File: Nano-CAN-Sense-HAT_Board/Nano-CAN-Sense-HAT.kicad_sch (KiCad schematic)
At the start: 42 parts, among them J1 Analog, J2 Digital, J3 Conn_02x04_Counter_Clockwise, J4 Conn_02x04_Counter_Clockwise, J5 Conn_01x05, J6 Conn_01x03, SW1 SW_Push, SW2 SW_Push, U1 LMC6484, U2 MCP2518FD-xQBB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

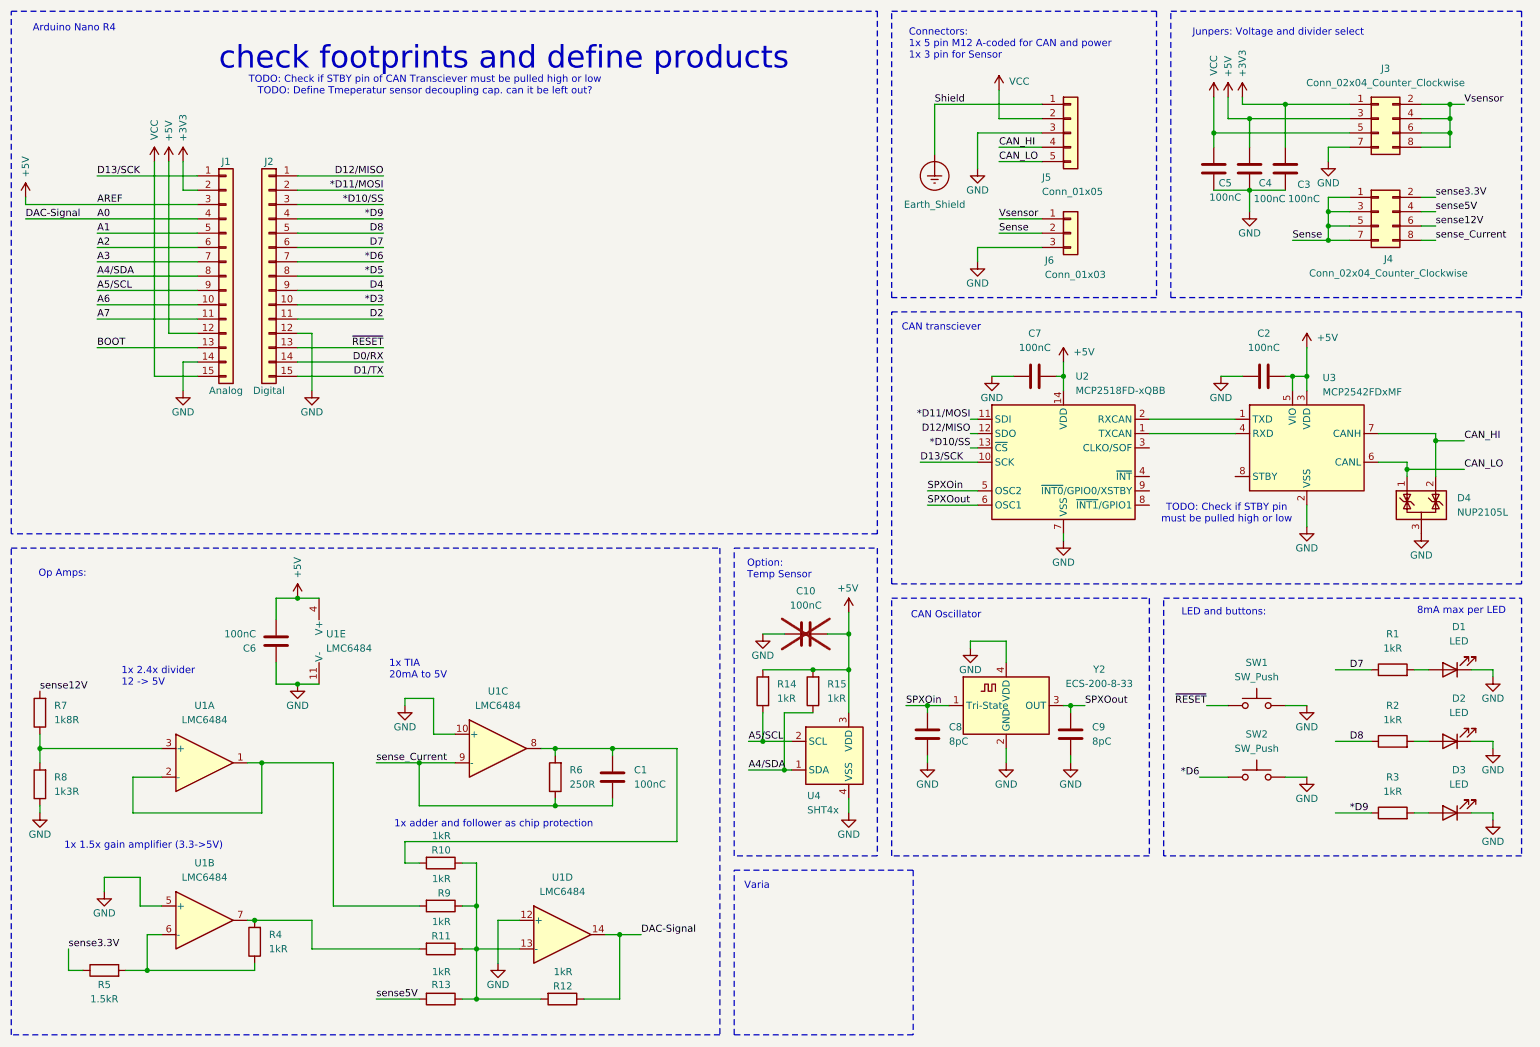
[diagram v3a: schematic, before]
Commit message: Added BOM, defined footprints
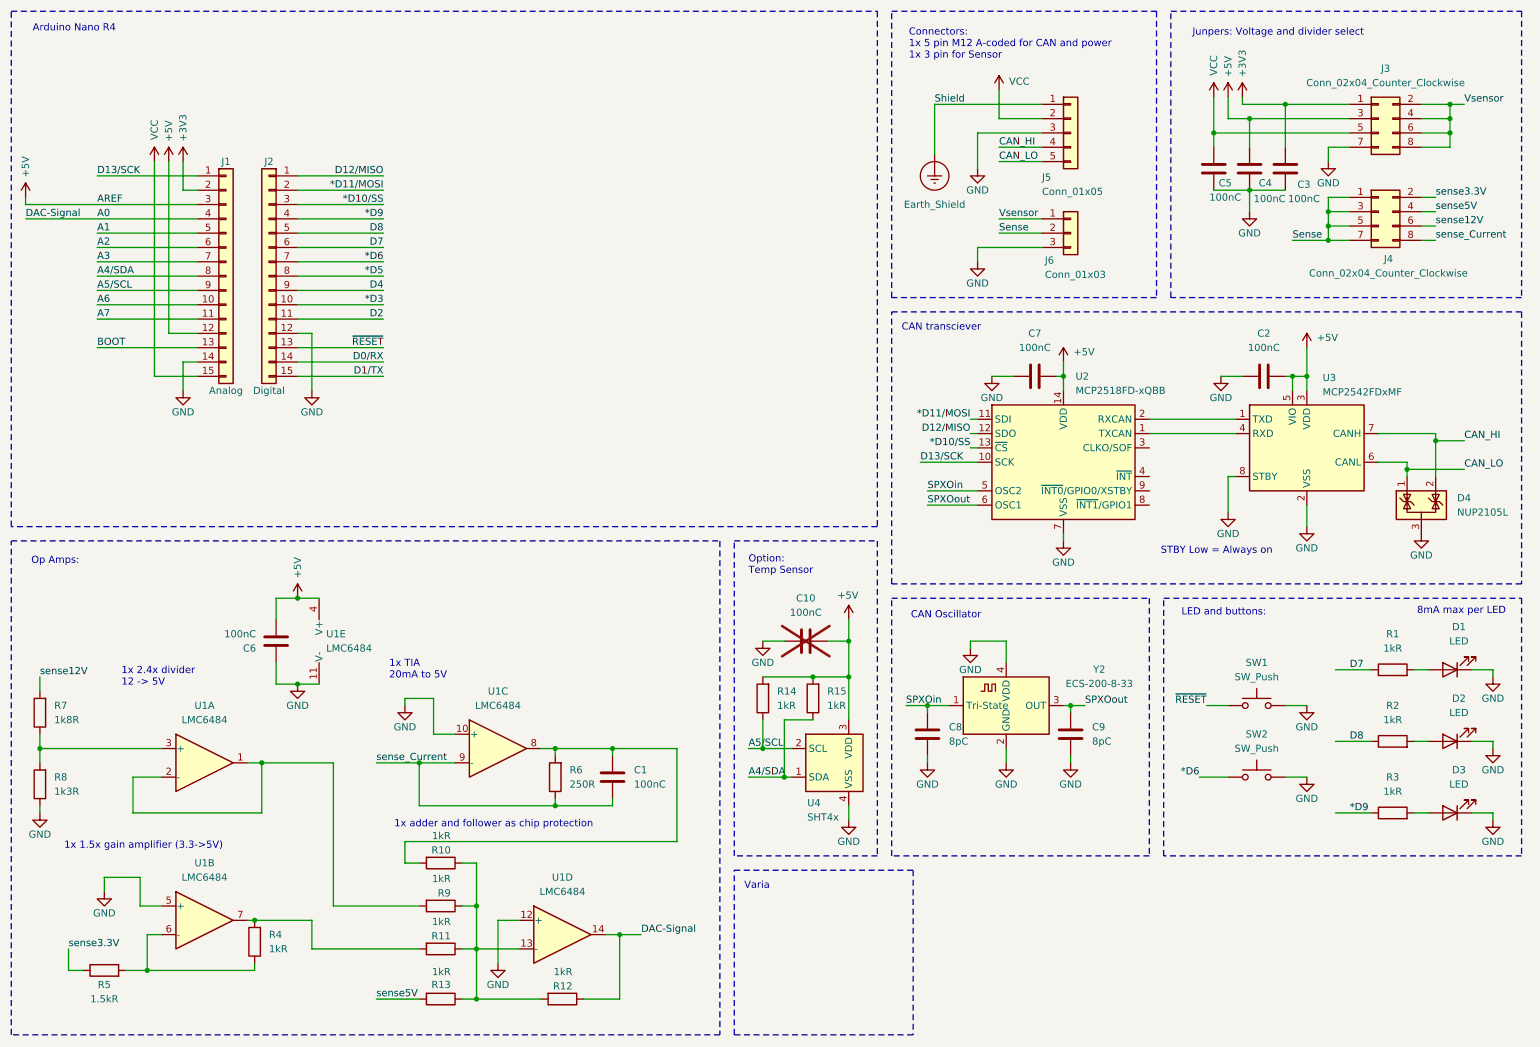
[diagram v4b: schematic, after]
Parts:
- C1, C2, C3, C4, C5, C6, C7, C8, C9, R1, R10, R11, R12, R13, R14, R15, R2, R3, R4, R5, R6, R7, R8, R9: Price (none) -> 0.03
- D1, D2, D3: Price (none) -> 0.06
- D4: Price (none) -> 0.15
- J1, J2, J3, J4, J5, J6: Price (none) -> 0.5
- SW1, SW2: Price (none) -> 0.8
- U1: Price (none) -> 2.8
- U2: Price (none) -> 1.8
- U3: Price (none) -> 1
- U4: Price (none) -> 1.7
- Y2: Price (none) -> 0.3
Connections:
- net GND: now also U3.8 (STBY)
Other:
- note added: "STBY Low = Always on"
- note removed: "TODO: Check if STBY pin must be pulled high or low"
- note removed: "TODO: Check if STBY pin of CAN Transciever must be pulled high or low TODO: Define Tmeperatur sensor decoupling cap. can it be left out?"
- note removed: "check footprints and define products"
- moved on the sheet: C10, R14, R15, U4

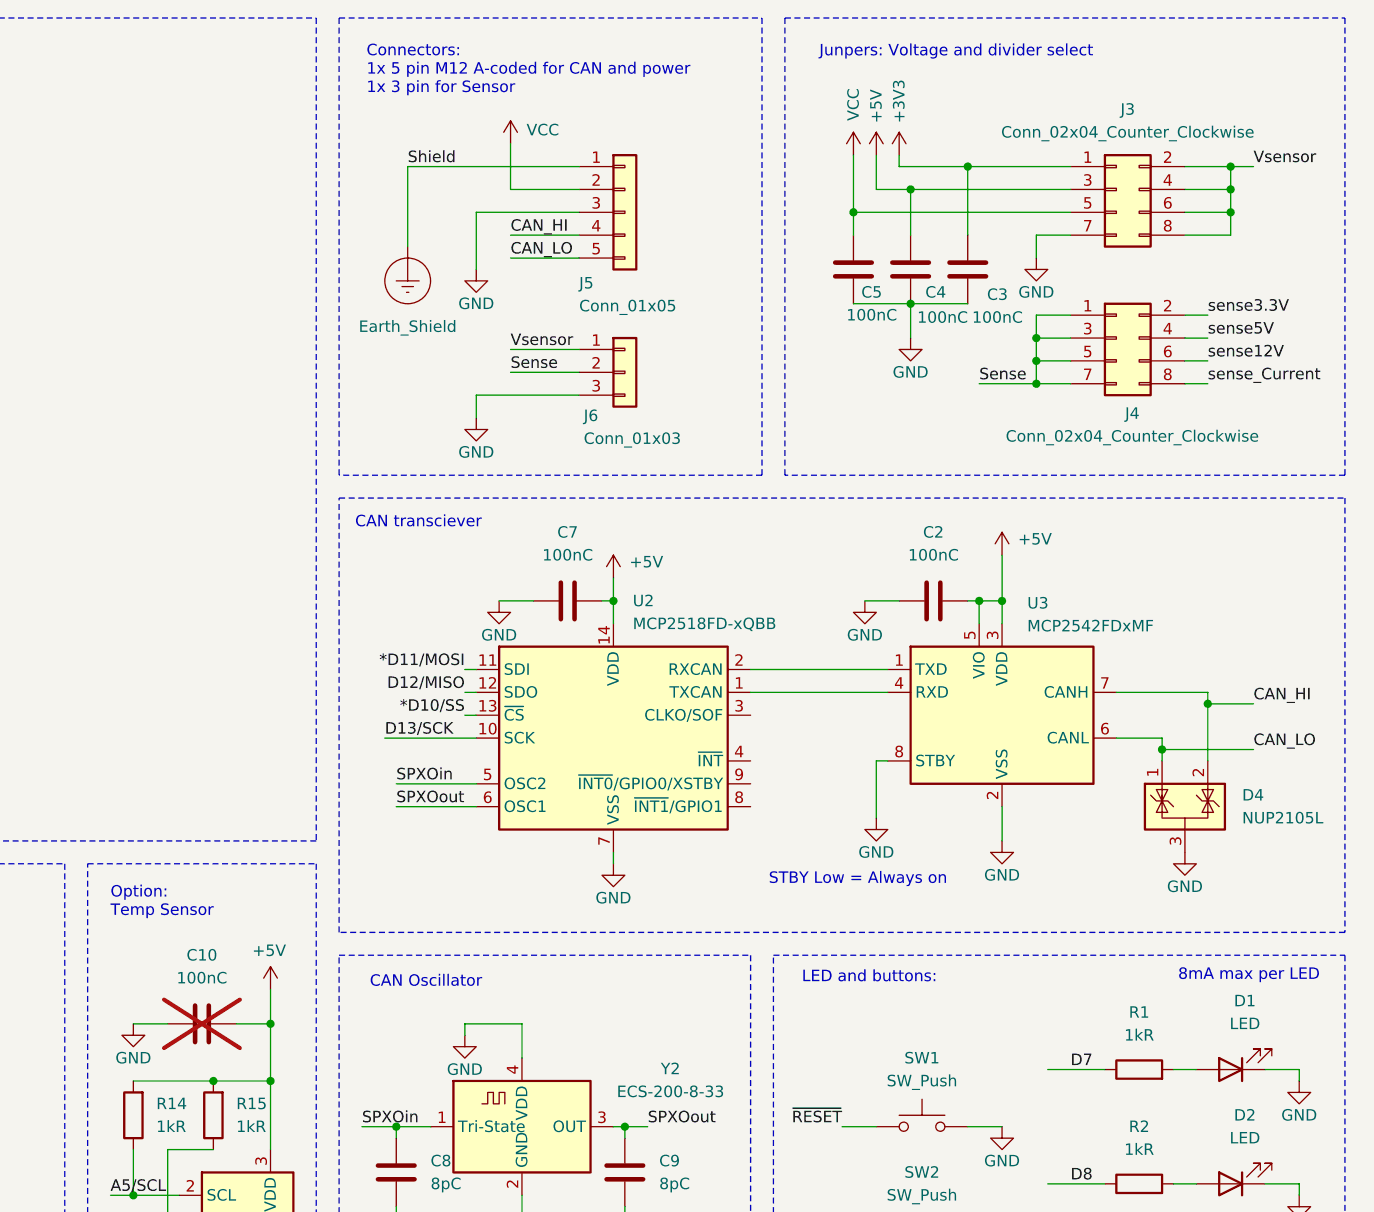
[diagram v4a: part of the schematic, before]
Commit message: Rodone all rounting, changed to 4-layer baord
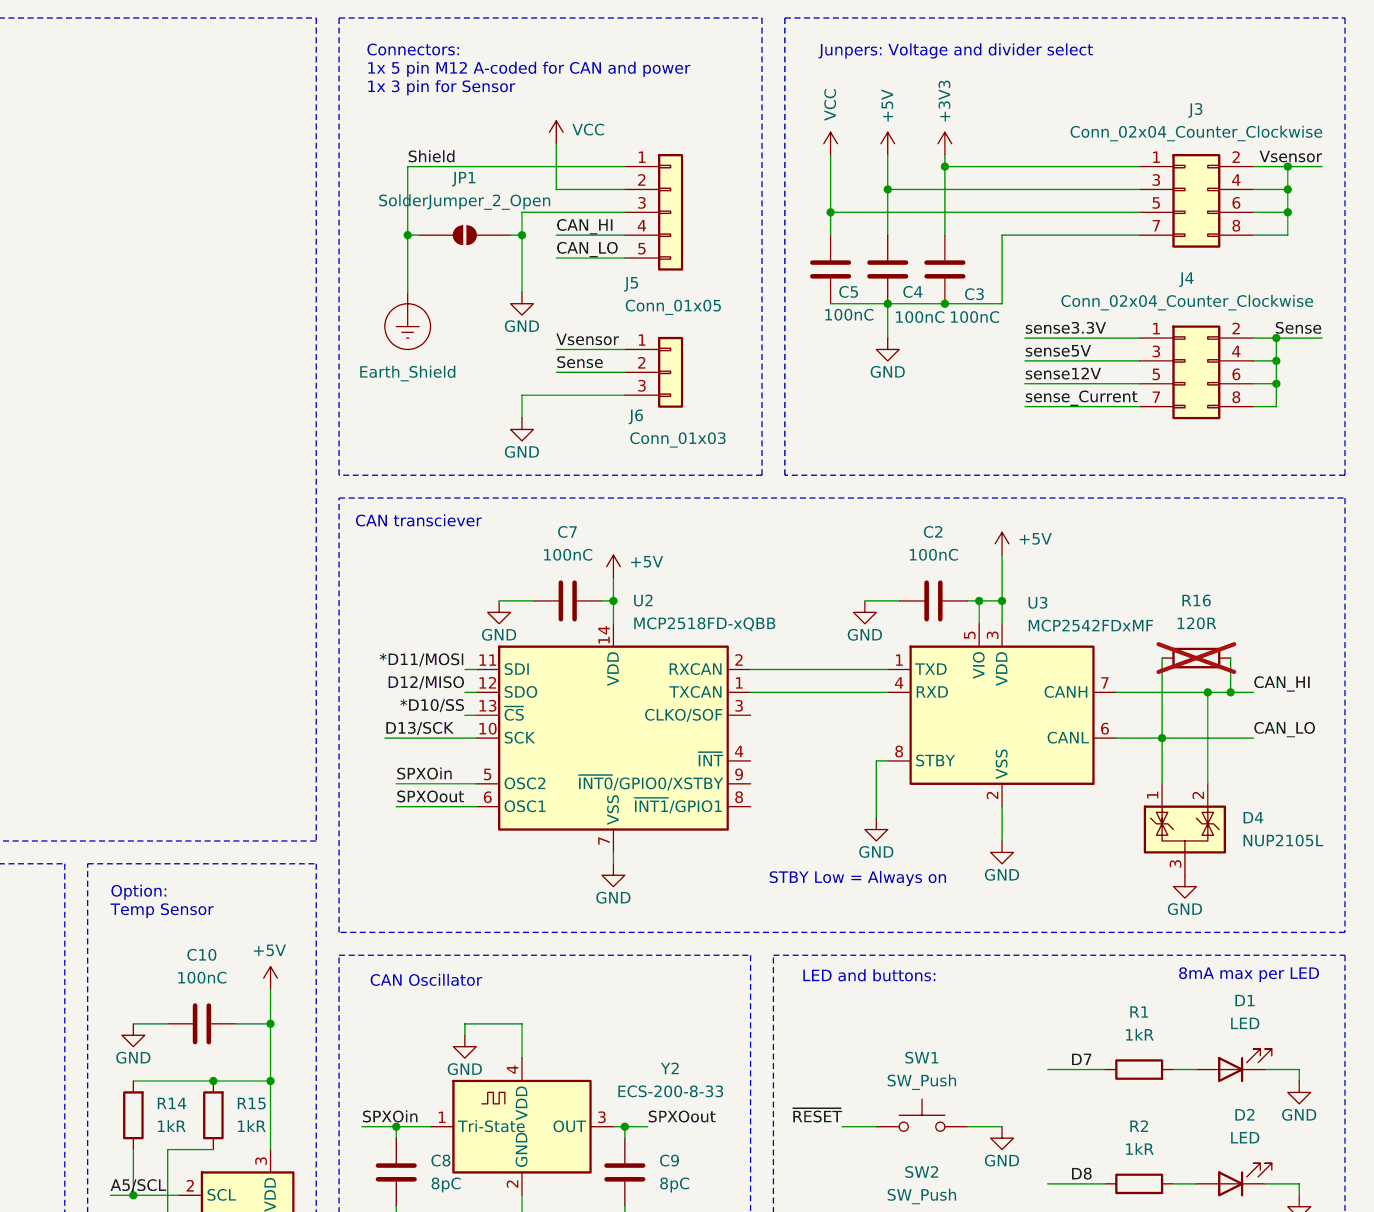
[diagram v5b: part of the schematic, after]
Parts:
- added JP1: SolderJumper_2_Open, Jumper:SolderJumper-2_P1.3mm_Open_TrianglePad1.0x1.5mm, symbol Jumper:SolderJumper_2_Open
- added R16: 120R, Resistor_SMD:R_0603_1608Metric, symbol Device:R
- C1, C2, C3, C4, C5, C6, C7, C8, C9: footprint Capacitor_SMD:C_0603_1608Metric_Pad1.08x0.95mm_HandSolder -> Capacitor_SMD:C_0603_1608Metric
- C10: footprint Capacitor_SMD:C_0603_1608Metric_Pad1.08x0.95mm_HandSolder -> Capacitor_SMD:C_0603_1608Metric; now fitted; now in the parts list
- D1, D2, D3: footprint LED_SMD:LED_0805_2012Metric_Pad1.15x1.40mm_HandSolder -> LED_SMD:LED_0805_2012Metric
- R1, R10, R11, R12, R13, R14, R15, R2, R3, R4, R5, R6, R7, R8, R9: footprint Resistor_SMD:R_0603_1608Metric_Pad0.98x0.95mm_HandSolder -> Resistor_SMD:R_0603_1608Metric
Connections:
- net CAN_HI: now also R16.1
- net CAN_LO: now also R16.2
- net Earth_Shield: now also JP1.1 (A)
- net GND: now also JP1.2 (B)
- net Sense: now also J4.2 (Pin_2), J4.4 (Pin_4), J4.6 (Pin_6), J4.8 (Pin_8); no longer J4.1 (Pin_1), J4.3 (Pin_3), J4.5 (Pin_5), J4.7 (Pin_7)
- net sense12V: now also J4.5 (Pin_5); no longer J4.6 (Pin_6)
- net sense3.3V: now also J4.1 (Pin_1); no longer J4.2 (Pin_2)
- net sense5V: now also J4.3 (Pin_3); no longer J4.4 (Pin_4)
- net sense_Current: now also J4.7 (Pin_7); no longer J4.8 (Pin_8)
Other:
- moved on the sheet: C3, C4, C5, D4, J3, J4, J5, J6

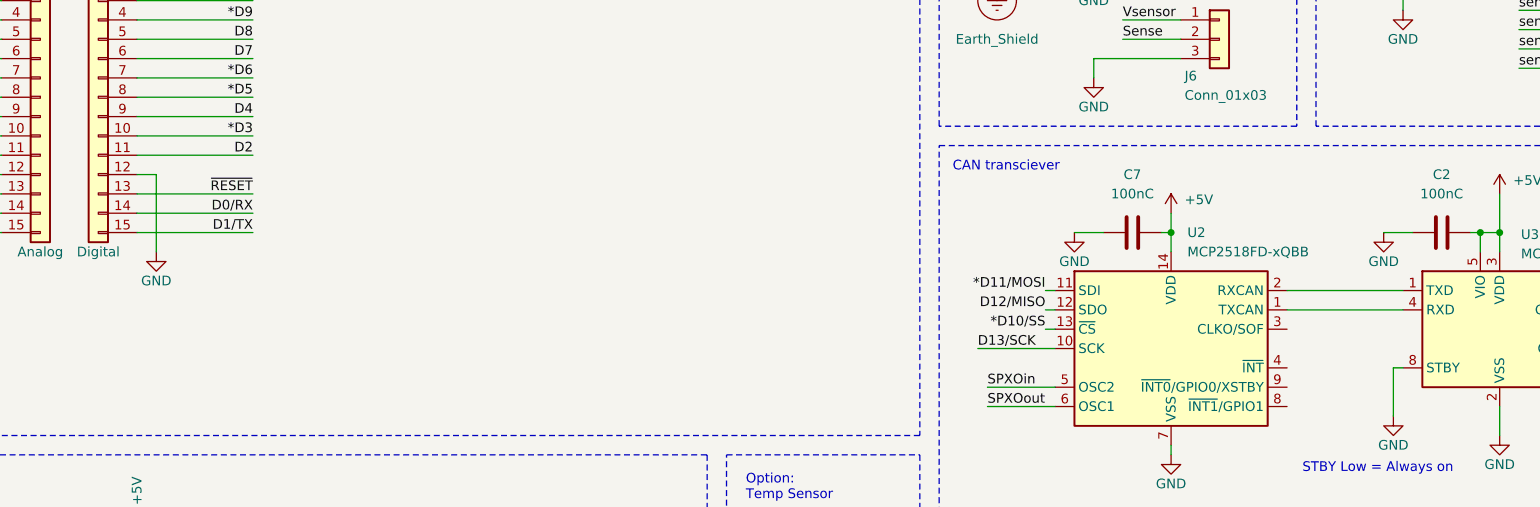
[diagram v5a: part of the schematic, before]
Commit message: Started draft coding Layout fixes
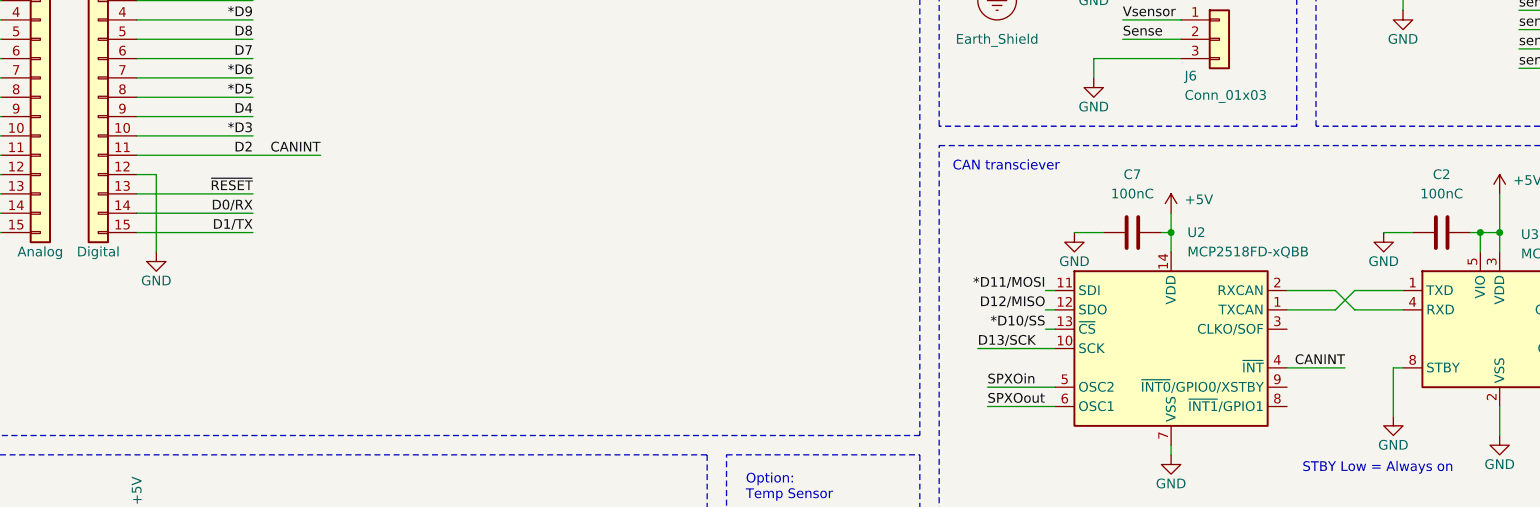
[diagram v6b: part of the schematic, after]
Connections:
- net D2 is gone; now on net CANINT: J2.11 (Pin_11)
- net at U3.1 (TXD): now also U2.1 (TXCAN); no longer U2.2 (RXCAN)
- net at U3.4 (RXD): now also U2.2 (RXCAN); no longer U2.1 (TXCAN)
- net CANINT: now reaches U2.4 (~{INT})
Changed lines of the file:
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@@
 	(wire
 		(pts
-			(xy 215.9 88.9) (xy 231.14 88.9)
-		)
-		(stroke
-			(width 0)
-			(type default)
-		)
-	)
-	(wire
-		(pts
 			(xy 46.99 45.72) (xy 44.45 45.72)
 		)
@@
 	(wire
 		(pts
+			(xy 215.9 86.36) (xy 222.25 86.36)
+		)
+		(stroke
+			(width 0)
+			(type default)
+		)
+	)
+	(wire
+		(pts
 			(xy 176.53 101.6) (xy 185.42 101.6)
 		)
@@
 	(wire
 		(pts
-			(xy 64.77 68.58) (xy 80.01 68.58)
+			(xy 64.77 68.58) (xy 88.9 68.58)
 		)
 		(stroke
@@
 	(wire
 		(pts
+			(xy 224.79 88.9) (xy 231.14 88.9)
+		)
+		(stroke
+			(width 0)
+			(type default)
+		)
+	)
+	(wire
+		(pts
 			(xy 57.15 182.88) (xy 57.15 184.15)
 		)
@@
 	(wire
 		(pts
+			(xy 215.9 88.9) (xy 222.25 88.9)
+		)
+		(stroke
+			(width 0)
+			(type default)
+		)
+	)
+	(wire
+		(pts
 			(xy 67.31 71.12) (xy 67.31 81.28)
 		)
@@
 	(wire
 		(pts
-			(xy 19.05 144.78) (xy 19.05 147.32)
+			(xy 224.79 86.36) (xy 231.14 86.36)
 		)
 		(stroke
@@
 	(wire
 		(pts
-			(xy 40.64 172.72) (xy 36.83 172.72)
+			(xy 19.05 144.78) (xy 19.05 147.32)
 		)
 		(stroke
@@
 	(wire
 		(pts
-			(xy 190.5 38.1) (xy 190.5 44.45)
+			(xy 40.64 172.72) (xy 36.83 172.72)
 		)
 		(stroke
@@
 	(wire
 		(pts
-			(xy 64.77 78.74) (xy 80.01 78.74)
+			(xy 190.5 38.1) (xy 190.5 44.45)
 		)
 		(stroke
 			(width 0)
-			(type solid)
+			(type default)
 		)
 	)
 	(wire
 		(pts
-			(xy 194.31 33.02) (xy 201.93 33.02)
+			(xy 64.77 78.74) (xy 80.01 78.74)
 		)
 		(stroke
 			(width 0)
-			(type default)
+			(type solid)
 		)
 	)
 	(wire
 		(pts
-			(xy 184.15 91.44) (xy 185.42 91.44)
+			(xy 194.31 33.02) (xy 201.93 33.02)
 		)
 		(stroke
@@
 	(wire
 		(pts
-			(xy 215.9 86.36) (xy 231.14 86.36)
+			(xy 184.15 91.44) (xy 185.42 91.44)
 		)
 		(stroke
@@
 	(wire
 		(pts
+			(xy 222.25 88.9) (xy 224.79 86.36)
+		)
+		(stroke
+			(width 0)
+			(type default)
+		)
+	)
+	(wire
+		(pts
 			(xy 16.51 48.26) (xy 46.99 48.26)
 		)
@@
 	(wire
 		(pts
+			(xy 224.79 88.9) (xy 222.25 86.36)
+		)
+		(stroke
+			(width 0)
+			(type default)
+		)
+	)
+	(wire
+		(pts
 			(xy 194.31 27.94) (xy 194.31 33.02)
 		)
@@
 	(wire
 		(pts
+			(xy 215.9 96.52) (xy 223.52 96.52)
+		)
+		(stroke
+			(width 0)
+			(type default)
+		)
+	)
+	(wire
+		(pts
 			(xy 190.5 129.54) (xy 190.5 125.73)
 		)
@@
 	)
 	(image
-		(at 124.46 60.96)
-		(scale 1.15517)
+		(at 128.27 64.77)
+		(scale 1.0773)
 		(data "iVBORw0KGgoAAAANSUhEUgAAA0YAAALtCAYAAAAMiHSBAAAABHNCSVQICAgIfAhkiAAAIABJREFU"
 			"eJzs3Xl8VPW9//HXmTX7DiGsSSBAICBQxF1woSq4VW0rIEtd23u1Xgva/hRbUGtbwWvtYntrbVUI"
@@
 		)
 	)
+	(label "CANINT"
+		(at 223.52 96.52 180)
+		(effects
+			(font
+				(size 1.27 1.27)
+			)
+			(justify right bottom)
+		)
+	)
 	(label "Sense"
 		(at 279.4 49.53 180)
@@
 		(effects
 			(font
+				(size 1.27 1.27)
+			)
+			(justify right bottom)
+		)
+	)
+	(label "CANINT"
+		(at 88.9 68.58 180)
+		(effects
+			(font
